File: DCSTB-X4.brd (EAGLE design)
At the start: 29 x 53 mm, 4 parts

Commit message: Changed board texts. Generated CAM files. Generated PDF schematics.
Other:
- board text added: "DCSTB-X4-0010 (c) Andriy Golovnya http://redscorp.net"
- board text removed: "DC-STB-X4-0010 (c) Andriy Golovnya http://redscorp.net"
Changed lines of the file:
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@@
 <circle x="15" y="4" radius="4.5" width="0.127" layer="51"/>
 <circle x="15" y="49" radius="4.5" width="0.127" layer="51"/>
-<text x="28" y="38" size="1.778" layer="22" font="vector" rot="MR270">DC-STB-X4-0010
+<text x="28" y="38" size="1.778" layer="22" font="vector" rot="MR270">DCSTB-X4-0010
 (c) Andriy Golovnya
 http://redscorp.net</text>

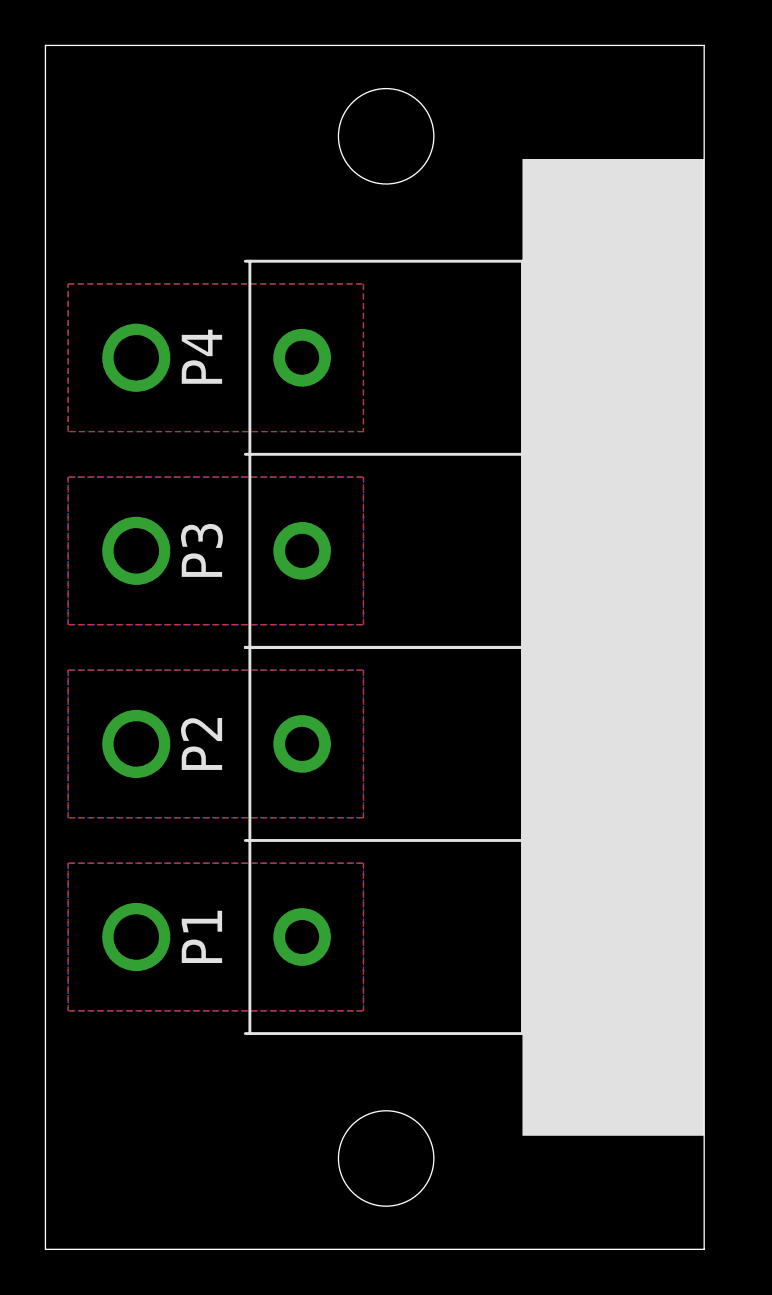
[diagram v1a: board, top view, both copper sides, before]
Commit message: Made boards a little bigger. Generated PNG preview. Generated CAM files.
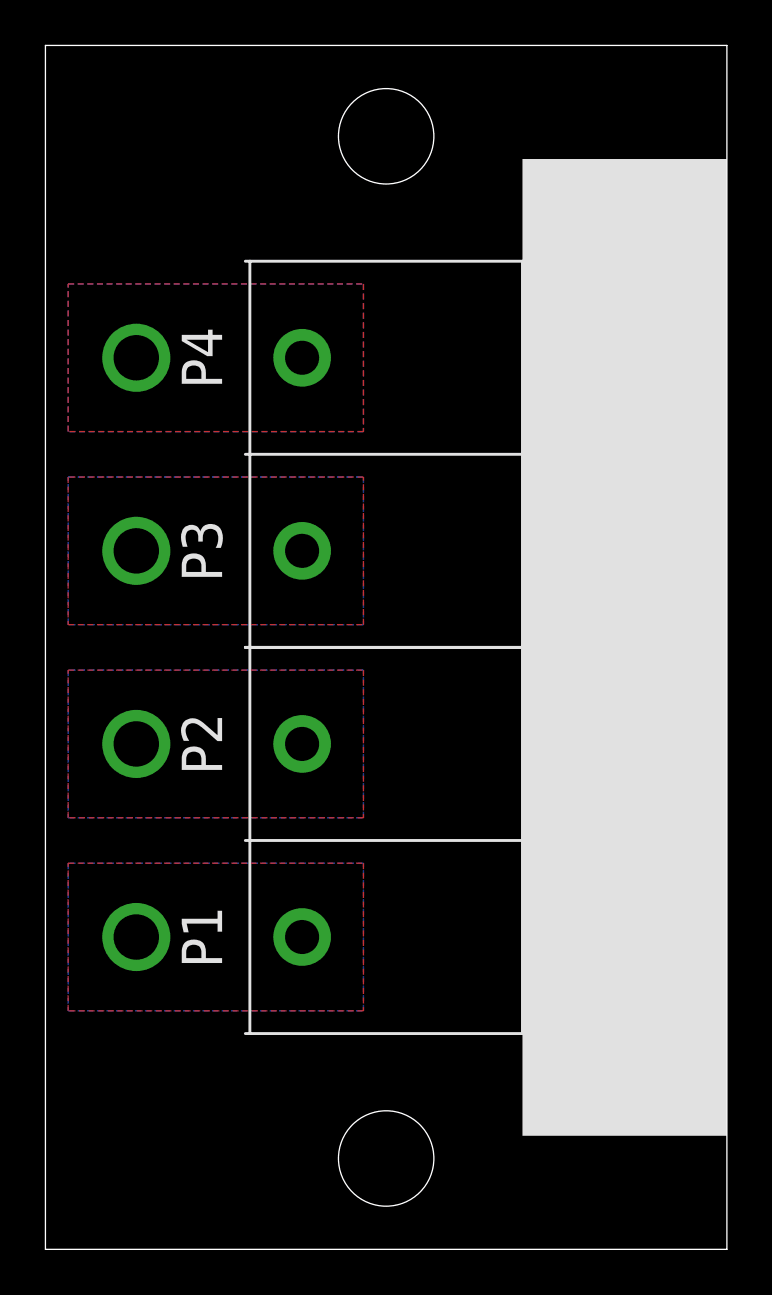
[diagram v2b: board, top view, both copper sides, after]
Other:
- board size 29 x 53 mm -> 30 x 53 mm
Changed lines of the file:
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@@
 <board>
 <plain>
-<wire x1="0" y1="0" x2="29" y2="0" width="0" layer="20"/>
-<wire x1="29" y1="0" x2="29" y2="53" width="0" layer="20"/>
-<wire x1="29" y1="53" x2="0" y2="53" width="0" layer="20"/>
+<wire x1="0" y1="0" x2="30" y2="0" width="0" layer="20"/>
+<wire x1="30" y1="0" x2="30" y2="53" width="0" layer="20"/>
+<wire x1="30" y1="53" x2="0" y2="53" width="0" layer="20"/>
 <wire x1="0" y1="53" x2="0" y2="0" width="0" layer="20"/>
 <hole x="15" y="4" drill="4.2"/>
@@
 <circle x="15" y="4" radius="4.5" width="0.127" layer="51"/>
 <circle x="15" y="49" radius="4.5" width="0.127" layer="51"/>
-<text x="28" y="38" size="1.778" layer="22" font="vector" rot="MR270">DCSTB-X4-0010
+<text x="29" y="38" size="1.778" layer="22" font="vector" rot="MR270">DCSTB-X4-0010
 (c) Andriy Golovnya
 http://redscorp.net</text>
-<rectangle x1="21" y1="5" x2="29" y2="48" layer="21"/>
+<rectangle x1="21" y1="5" x2="30" y2="48" layer="21"/>
 <text x="6" y="13.75" size="1.778" layer="21" font="vector" rot="R90" align="top-center">P1</text>
 <text x="6" y="22.25" size="1.778" layer="21" font="vector" rot="R90" align="top-center">P2</text>
